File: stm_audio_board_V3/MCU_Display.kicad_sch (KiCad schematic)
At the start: 14 parts, among them J18 Conn_01x16_ILI9341, SW1 SW_SPST, U17 W25Q128JVS, U7 STM32H723ZGTx, Y2 X1E0000210132

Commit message: PCB design is finished
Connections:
- net I2C_SCL: now reaches U7.100 (PA8)
- net I2C_SDA: now reaches U7.99 (PC9)

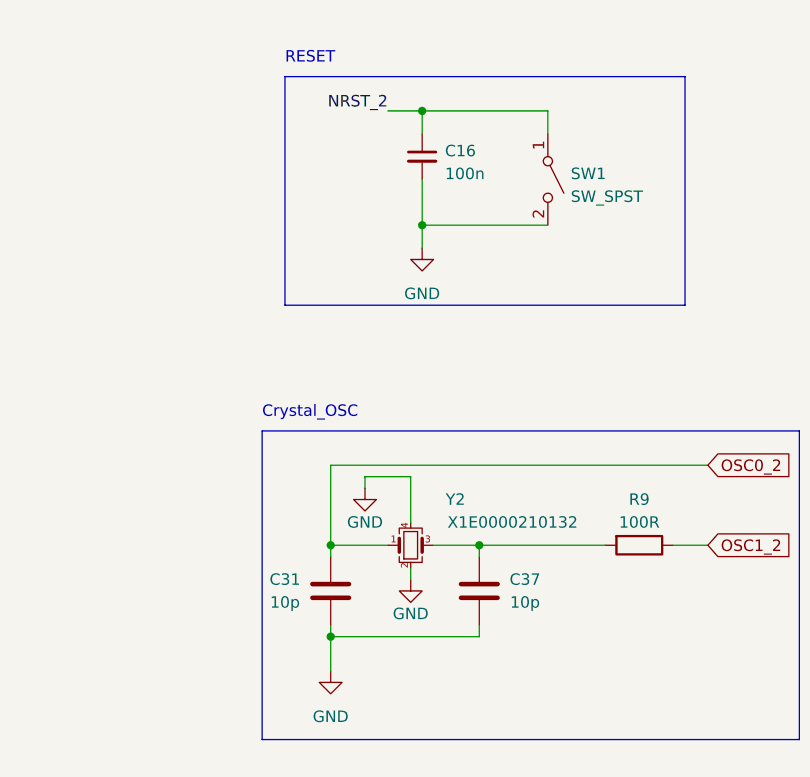
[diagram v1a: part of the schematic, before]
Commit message: minor changes to components
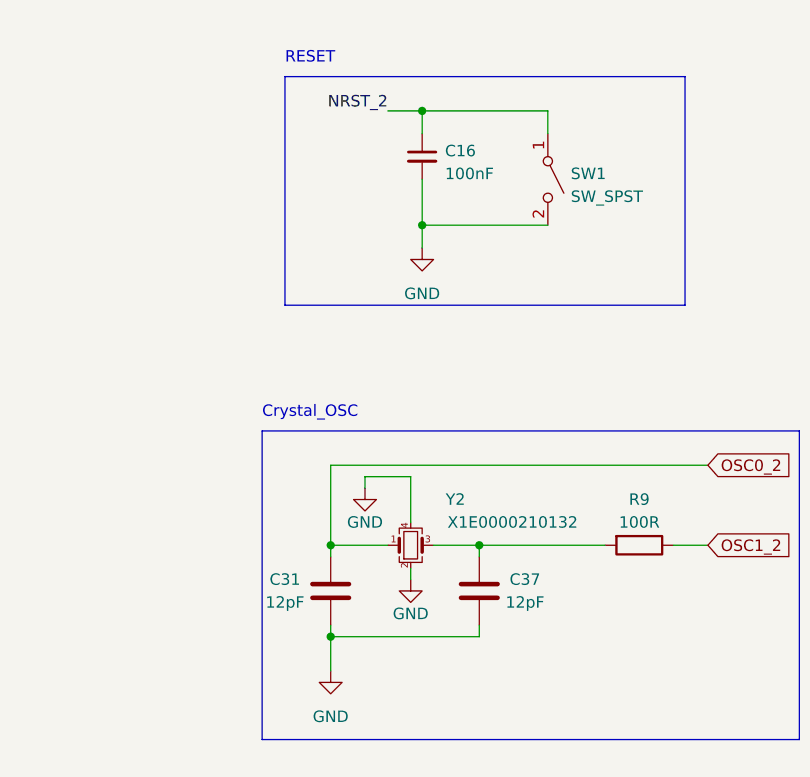
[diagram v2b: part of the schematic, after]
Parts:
- C15: JLCPCB (none) -> C377773; LCSC Part (none) -> C377773
- C16: value 100n -> 100nF; JLCPCB (none) -> C14663; LCSC Part (none) -> C14663
- C31, C37: value 10p -> 12pF; JLCPCB (none) -> C38523; LCSC Part (none) -> C38523
- D10: LCSC Part (none) -> C2297
- R2: JLCPCB (none) -> C25804; LCSC Part (none) -> C25804
- R9: footprint Resistor_SMD:R_0603_1608Metric_Pad0.98x0.95mm_HandSolder -> Resistor_SMD:R_0603_1608Metric; JLCPCB (none) -> C21190; LCSC Part (none) -> C21190
- R9: JLCPCB (none) -> C22775; LCSC Part (none) -> C22775
- U17: JLCPCB (none) -> C97521; LCSC Part (none) -> C97521
- U7: LCSC Part (none) -> C730146
- Y2: LCSC Part (none) -> C9006
